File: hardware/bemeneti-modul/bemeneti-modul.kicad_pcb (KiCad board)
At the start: 4 copper layers, 103 x 86.5 mm, 156 parts, among them J1 DEBUG, J2 BUS_IN, J3 BUS_OUT, J301 IN0, J302 IN1, J303 IN2, J304 IN3, J305 IN4, J306 IN5, J307 IN6, J308 IN7, J309 IN8, J310 IN9, J311 IN10, J312 IN11, J313 IN12, J314 IN13, J315 IN14, J316 IN15, J320 I2C KÜLSŐ, J4 BŐVÍTŐ, U2 TCAN1044AVDRQ1, U3 ESD2CAN24-Q1, U301 AP2112K-3.3TRG1, U302 HDC3020DEFR, U303 TPD4E05U06DQAR, U304 TPD4E05U06DQAR, U305 TPD4E05U06DQAR, U306 TPD4E05U06DQAR, U307 TPD4E05U06DQAR, U5 AP2112K-3.3TRG1, U6 STM32F303RET6, Y1 8MHz

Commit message: Hardver: szakértői javítások (D74–D77), STM32L433 + SN65HVD230 + GND-ági polaritásvédelem (D78–D81), teljes ellenőrzés
- D74–D77: busz-GND ellenállás, CAN-fojtó-hely, TVS a +5V_BUCK-on és a VUSB-n, bemenetvédelem,
  230 V-os és antenna-tiltás a NYÁK-on, SCT-jack footprint
- D78–D80: modul-MCU STM32L433RCT3 (VIN_SENSE PB1, LED: TIM15/TIM16, I_SENSE PA3), modul-transceiver
  SN65HVD230, N-FET a GND-ágban (vezérlő Q1, LED Q201, relé Q100), MCP9701A, táp-LED a +5V-ról,
  2 oz a LED-/relémodulon, AP2112K marad; D81 javaslat (TPD4E02B04 a bemeneteken)
- CubeMX-projektek L433-ra, fejsoros kódgenerálással ellenőrizve (minden periféria inicializálódik)
- gen/ellenorzes.py (ERC, láb ↔ pad, modulmag, CubeMX, polaritásvédelem, NYÁK ↔ rajz, DRC) – 0 hiba
- gen/bom.sh + bom/*.csv darabjegyzék; docs/komponenslista.md a konzulensnek
- kontextus: DONTESEK D74–D81, specifikációk, ATTEKINTES, NAPLO, beszerzési lista; alkatrészkészlet-jegyzet (claude.ai)

Co-Authored-By: Claude Opus 5.5 <noreply@anthropic.com>
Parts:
- removed C17: 100n, Capacitor_SMD:C_0603_1608Metric
- added JP2: áthidaló, Jumper:SolderJumper-2_P1.3mm_Bridged_RoundedPad1.0x1.5mm, F.Cu at (125.8, 117.2)
- added JP3: áthidaló, Jumper:SolderJumper-2_P1.3mm_Bridged_RoundedPad1.0x1.5mm, F.Cu at (114.3, 117.2)
- added L1: DNP, Inductor_SMD:L_CommonModeChoke_Coilank_ACM3225, F.Cu at (120.1, 122.0)
- added R390: 0R, Resistor_SMD:R_1206_3216Metric, F.Cu at (125.3, 109.7)
- R310, R311, R312, R313, R314, R315, R316, R317, R318, R319, R320, R321, R322, R323, R324, R325: value 1k -> 10k
- U2: value TCAN1044AVDRQ1 -> SN65HVD230D
- U6: value STM32F303RET6 -> STM32L433RCT3
- moved F305 75.8 mm to (197.3, 109.2), turned to 0 degrees
- moved F302 66.8 mm to (105.8, 177.2)
- moved C305 65.3 mm to (101.8, 177.0), turned to 90 degrees
- moved C307 59.7 mm to (181.5, 177.8), turned to 0 degrees
- moved C304 56.5 mm to (154.5, 108.8)
- moved R8 46.7 mm to (147.5, 120.8)
- moved C18 46.1 mm to (141.5, 163.3)
- moved C13 44.1 mm to (129.8, 147.0)
- moved C14 44.1 mm to (129.8, 139.0)
- moved C7 44.0 mm to (147.5, 164.8)
- moved C4 42.2 mm to (136.3, 158.5), turned to 90 degrees
- moved C19 40.4 mm to (156.0, 121.3)
- moved D5 40.0 mm to (156.7, 124.2)
- moved C330 39.5 mm to (142.5, 123.8)
- moved C306 39.3 mm to (131.5, 177.8), turned to 0 degrees
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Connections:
- C18 pad 1: +5V -> +3V3
- C19 pad 1: +5V -> +3V3
- J2 pad 2: GND -> /GND_BUS
- J3 pad 2: GND -> /GND_BUS
- R330 pad 2: /IN0 -> Net-(J301-Pin_3)
- R331 pad 2: /IN1 -> Net-(J302-Pin_3)
- R332 pad 2: /IN2 -> Net-(J303-Pin_3)
- R333 pad 2: /IN3 -> Net-(J304-Pin_3)
- R334 pad 2: /IN4 -> Net-(J305-Pin_3)
- R335 pad 2: /IN5 -> Net-(J306-Pin_3)
- R336 pad 2: /IN6 -> Net-(J307-Pin_3)
- R337 pad 2: /IN7 -> Net-(J308-Pin_3)
- R338 pad 2: /IN8 -> Net-(J309-Pin_3)
- R339 pad 2: /IN9 -> Net-(J310-Pin_3)
- R340 pad 2: /IN10 -> Net-(J311-Pin_3)
- R341 pad 2: /IN11 -> Net-(J312-Pin_3)
- R342 pad 2: /IN12 -> Net-(J313-Pin_3)
- R343 pad 2: /IN13 -> Net-(J314-Pin_3)
- R344 pad 2: /IN14 -> Net-(J315-Pin_3)
- R345 pad 2: /IN15 -> Net-(J316-Pin_3)
- R8 pad 1: +3V3 -> +5V
- U2 pad 3: +5V -> +3V3
- U2 pad 5: +3V3 -> unconnected-(U2-Vref-Pad5)
- U2 pad 6: /modulmag/CAN_L -> /modulmag/CAN_L_T
- U2 pad 7: /modulmag/CAN_H -> /modulmag/CAN_H_T
- U6 pad 27: unconnected-(U6-PB1-Pad27) -> /modulmag/PB1
- U6 pad 37: /modulmag/PC6 -> unconnected-(U6-PC6-Pad37)
- U6 pad 38: /modulmag/PC7 -> unconnected-(U6-PC7-Pad38)
- U6 pad 39: /modulmag/PC8 -> unconnected-(U6-PC8-Pad39)

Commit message: Hardver: determinisztikus UUID-k – a NYÁK-footprintek újra a rajzi szimbólumokra mutatnak
- kigen: a szimbólum-UUID a projekt + hivatkozási jel alapján (uuid5), a többi elemé laponként sorszámból –
  két generálás bájtra azonos fájlt ad, és az újragenerálás nem töri el a „Update PCB from Schematic”-ot (D67)
- a négy NYÁK újragenerálva: mind a 581 footprint a saját szimbólumára mutat (előtte egy sem)
- ellenorzes.py: új ellenőrzés a NYÁK ↔ rajz szimbólum-kapcsolatra; teljes futás: 0 hiba
- README, NAPLO

Co-Authored-By: Claude Opus 5.5 <noreply@anthropic.com>
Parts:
- moved R1 56.6 mm to (170.3, 154.5), turned to 90 degrees
- moved C18 44.4 mm to (156.0, 121.3)
- moved R4 42.9 mm to (132.3, 150.5)
- moved R2 42.4 mm to (135.3, 130.5)
- moved C14 41.4 mm to (165.0, 160.8), turned to 0 degrees
- moved R10 37.0 mm to (168.5, 127.3), turned to 0 degrees
- moved R8 35.1 mm to (129.8, 151.0), turned to 90 degrees
- moved R3 35.0 mm to (170.3, 130.5)
- moved R11 32.0 mm to (136.5, 127.3)
- moved C15 23.6 mm to (141.5, 163.3)
- moved D3 21.1 mm to (132.8, 130.5), turned to 90 degrees
- moved C8 20.9 mm to (129.8, 147.0), turned to 90 degrees
- moved F304 20.5 mm to (197.3, 177.2)
- moved C307 19.8 mm to (201.3, 177.0), turned to 90 degrees
- moved FB1 17.7 mm to (147.5, 120.8), turned to 0 degrees
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
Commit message: Hardver: legolcsóbb beszerzés (D84) – Hestore + DigiKey, a rajz a kapható típusokra igazítva; beszerzési lista
- gen/beszerzes.py → bom/beszerzes.csv: BOM-tételenként forrás, Hestore-kód, nettó ár, készlet
- J1/J100 Degson DG250, J201 DG128 (15 A), J202–J204 KF128, F201 15 A; L1/L3 HPI0630 (saját footprint);
  R209 CRE2512; C40/C41 12 pF; ESP32-C6-WROOM-1-N8; SS56C, BAT54HT1G, STPS3L60U, BLM18EG221
- NYÁK-ok újragenerálva (a layout még nem indult el); bekötés változatlan, ellenorzes.py: 0 hiba
- SAMPLE-KERESEK: az NTMFS5C604NL nincs kézben (javítva)

Co-Authored-By: Claude Opus 5.5 <noreply@anthropic.com>
Claude-Session: https://claude.ai/code/session_01KVtZMUPbtveTXy9VyJshyt
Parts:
- FB1: value ferrit ≤0,1Ω -> BLM18EG221
- moved C305 112.8 mm to (191.5, 108.8), turned to 0 degrees
- moved F302 105.8 mm to (186.8, 109.2)
- moved C306 19.5 mm to (151.0, 177.8)
- moved C307 18.8 mm to (182.5, 177.8), turned to 0 degrees
- moved R390 17.5 mm to (107.8, 109.7)
- moved F303 10.0 mm to (146.3, 177.2)
- moved F304 10.0 mm to (187.3, 177.2)

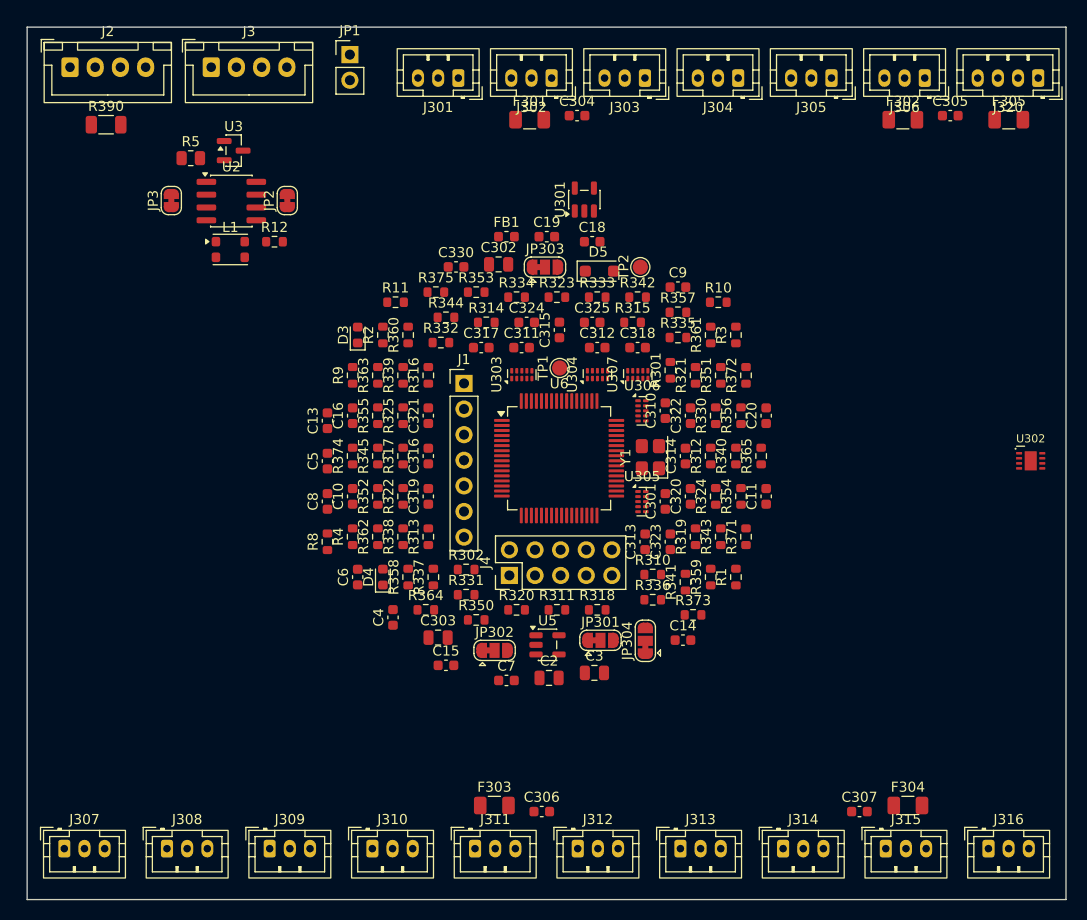
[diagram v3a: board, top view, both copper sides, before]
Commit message: Hardver: layout-előkészítés (D86) – JLC-szabályok és via-méretek, modulmag-blokk, a modulok elrendezése
- laponként .kicad_dru: JLC 4 réteg / 1 oz; via 0,3/0,45 (jel), 0,4/0,7 (táp), 0,6/1,0 mm (15 A); 230 V ↔ SELV 8 mm
- modulmag-blokk mindhárom modulon azonos relatív elrendezéssel (átvihető layout), 0,25 mm-es rács
- a sorkapcsok a Gainta D4MG fedélfurataira igazítva (5,08 mm), a kötött helyű alkatrészek zárolva
- LED-modul: LED-sor, meghajtók, FET-sor; relé: betáp és LED-sor; bemeneti: csatornánkénti oszlopok, ESD-sor
- lábhoz rendelés: hidegítők a tápjukhoz, gate-ellenállások a gate-hez; a vezérlő elrendezése még hátra (U4)
- docs/d4mg.pdf: a ház rajza; ellenorzes.py: 0 hiba

Co-Authored-By: Claude Opus 5.5 <noreply@anthropic.com>
Claude-Session: https://claude.ai/code/session_01KVtZMUPbtveTXy9VyJshyt
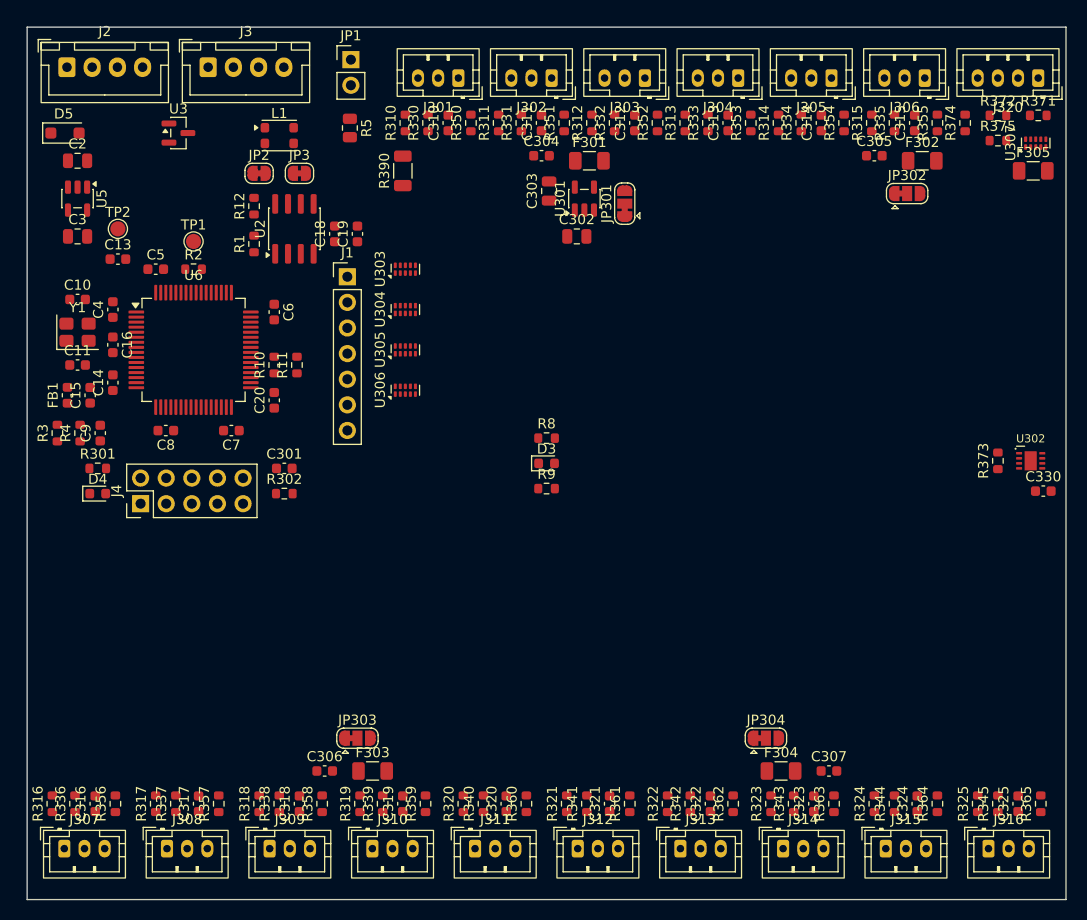
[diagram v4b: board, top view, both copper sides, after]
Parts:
- moved R356 73.0 mm to (108.8, 177.0)
- moved R345 70.5 mm to (196.2, 177.0)
- moved C11 69.5 mm to (105.0, 133.5), turned to 0 degrees
- moved C2 69.4 mm to (105.0, 113.2)
- moved R374 69.1 mm to (193.0, 109.5)
- moved R325 68.7 mm to (194.2, 177.0)
- moved R3 68.0 mm to (103.0, 140.2)
- moved C3 67.1 mm to (105.0, 120.8)
- moved R357 66.7 mm to (119.0, 177.0), turned to 90 degrees
- moved R344 65.6 mm to (186.0, 177.0), turned to 90 degrees
- moved U5 64.3 mm to (105.0, 117.0), turned to -90 degrees
- moved C325 63.7 mm to (198.2, 177.0), turned to 90 degrees
- moved R355 62.6 mm to (190.2, 109.5)
- moved C330 62.3 mm to (200.8, 146.0)
- moved R363 62.0 mm to (180.0, 177.0)
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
